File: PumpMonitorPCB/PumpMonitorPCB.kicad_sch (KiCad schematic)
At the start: 7 parts

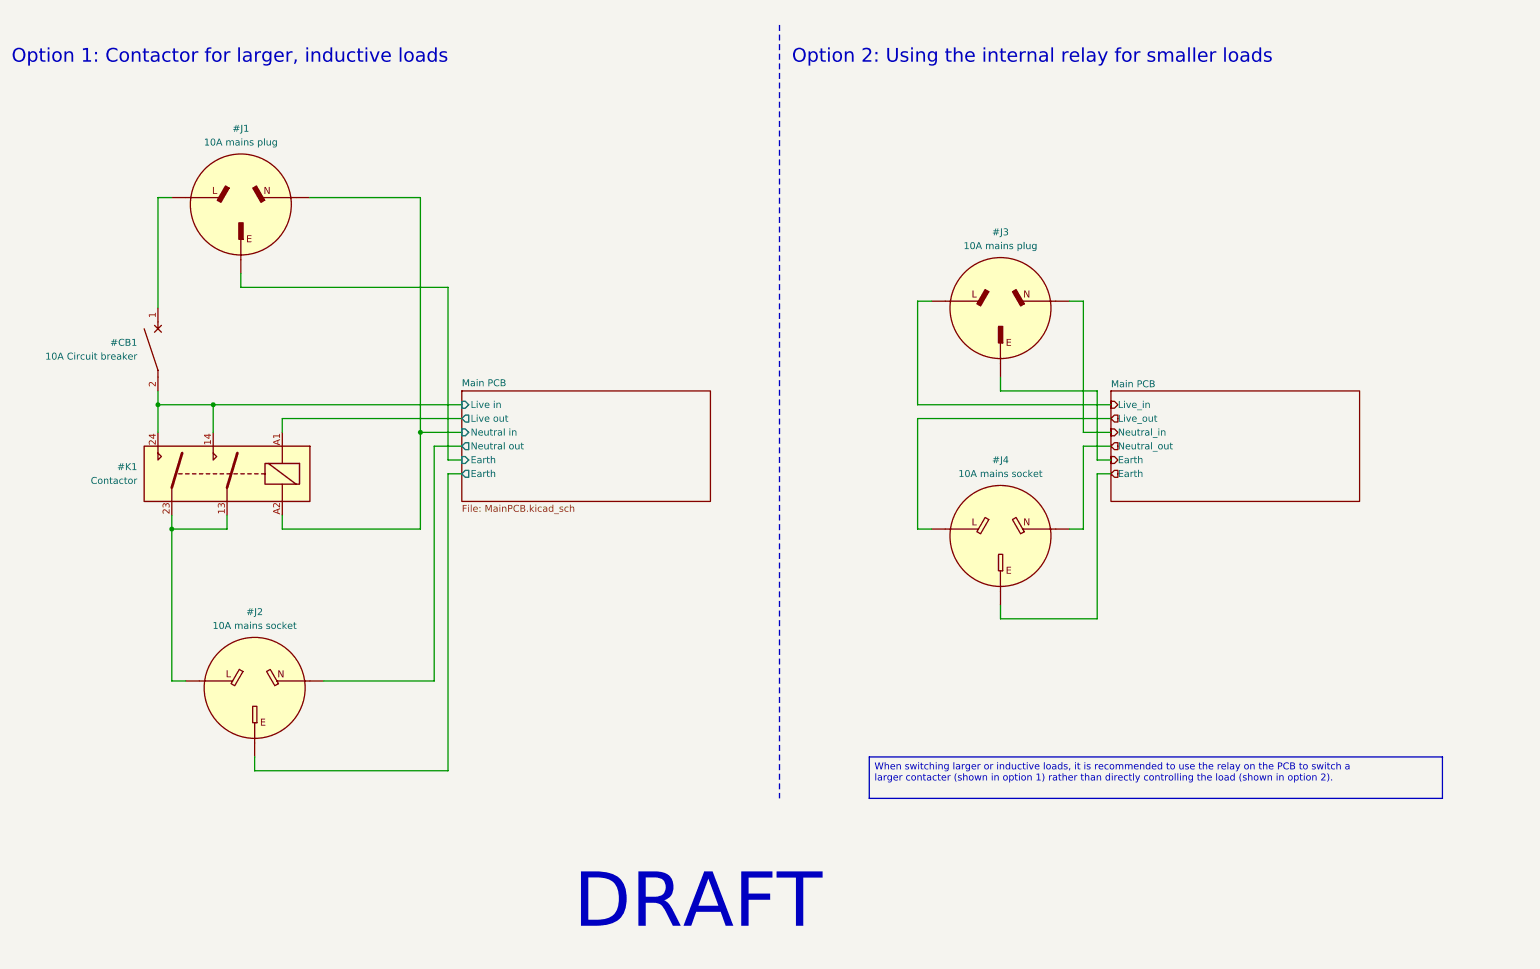
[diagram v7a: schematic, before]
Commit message: Rejigged auxilliary connectors, experimetning with kiclearance.
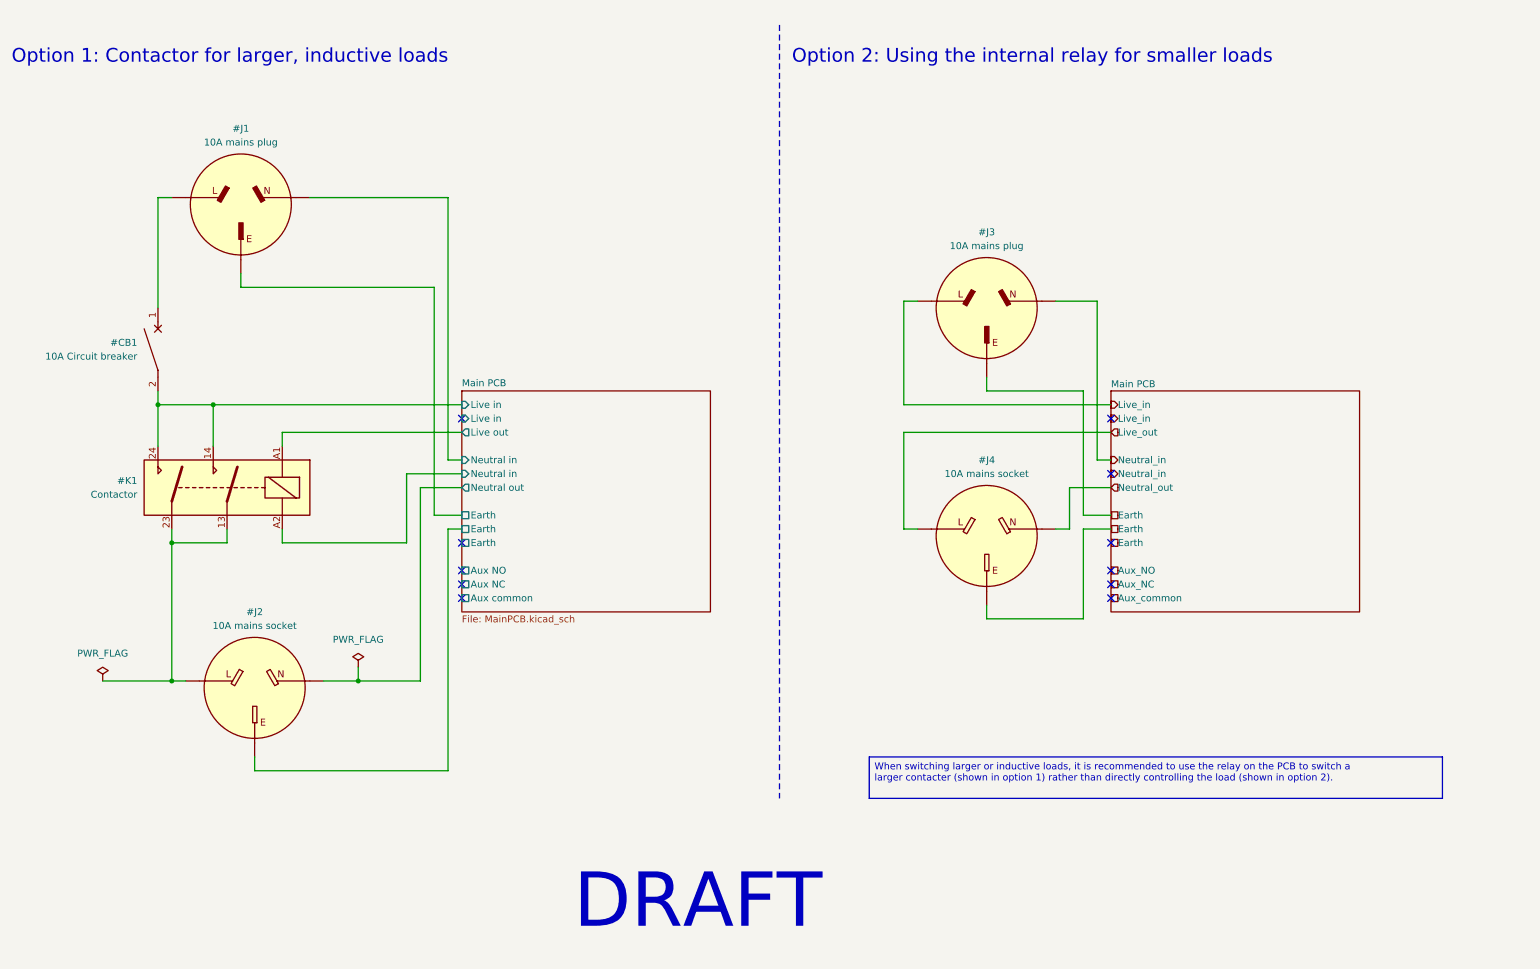
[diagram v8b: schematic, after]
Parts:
- renumbered #MOD1 to #MainPCB1
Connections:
- net Main PCB/Earth is gone; now on net Main PCB/Earth: #J2.3 (Earth)
- net Main PCB/Earth: no longer #J1.3 (Earth)
- net Main PCB/Neutral in: no longer #J1.2 (Neutral)
- net at #MainPCB1.2 (Live_in): no longer #J4.1 (Live)
- net at #MainPCB1.3 (Live_out): now also #J4.1 (Live); no longer #J3.2 (Neutral)
- net at #MainPCB1.4 (Neutral_in): now also #J3.2 (Neutral); no longer #J4.2 (Neutral)
- net at #MainPCB1.5 (Neutral_in): no longer #J3.3 (Earth)
- net at #MainPCB1.6 (Neutral_out): now also #J4.2 (Neutral); no longer #J4.3 (Earth)
- new net: #J3.3 (Earth), #MainPCB1.7 (Earth)
- new net: #J4.3 (Earth), #MainPCB1.8 (Earth)
- new net Main PCB/Earth: #J1.3 (Earth)
- new net Main PCB/Neutral in: #J1.2 (Neutral)
- no-connect marks 0 -> 11
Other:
- sheet Main PCB ports: added Aux NC, Aux NO, Aux common; removed none
